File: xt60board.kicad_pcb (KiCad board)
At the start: 2 copper layers, 50.8 x 86.4 mm, 13 parts, among them J1 XT60, J10 XT60, J11 XT60, J12 XT60, J2 XT60, J3 XT60, J4 XT60, J5 XT60, J6 XT60, J7 XT60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

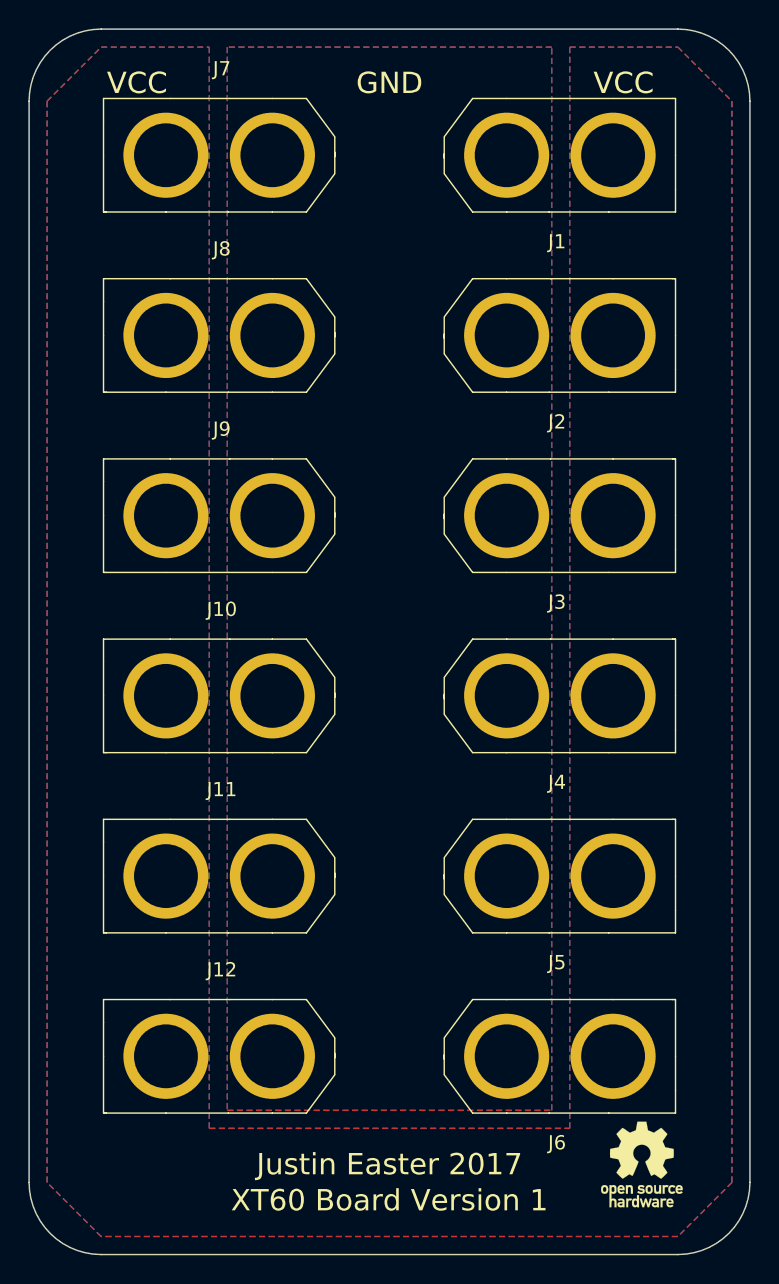
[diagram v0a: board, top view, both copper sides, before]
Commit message: Version 2
Shrank board size to reduce manufacturing cost.
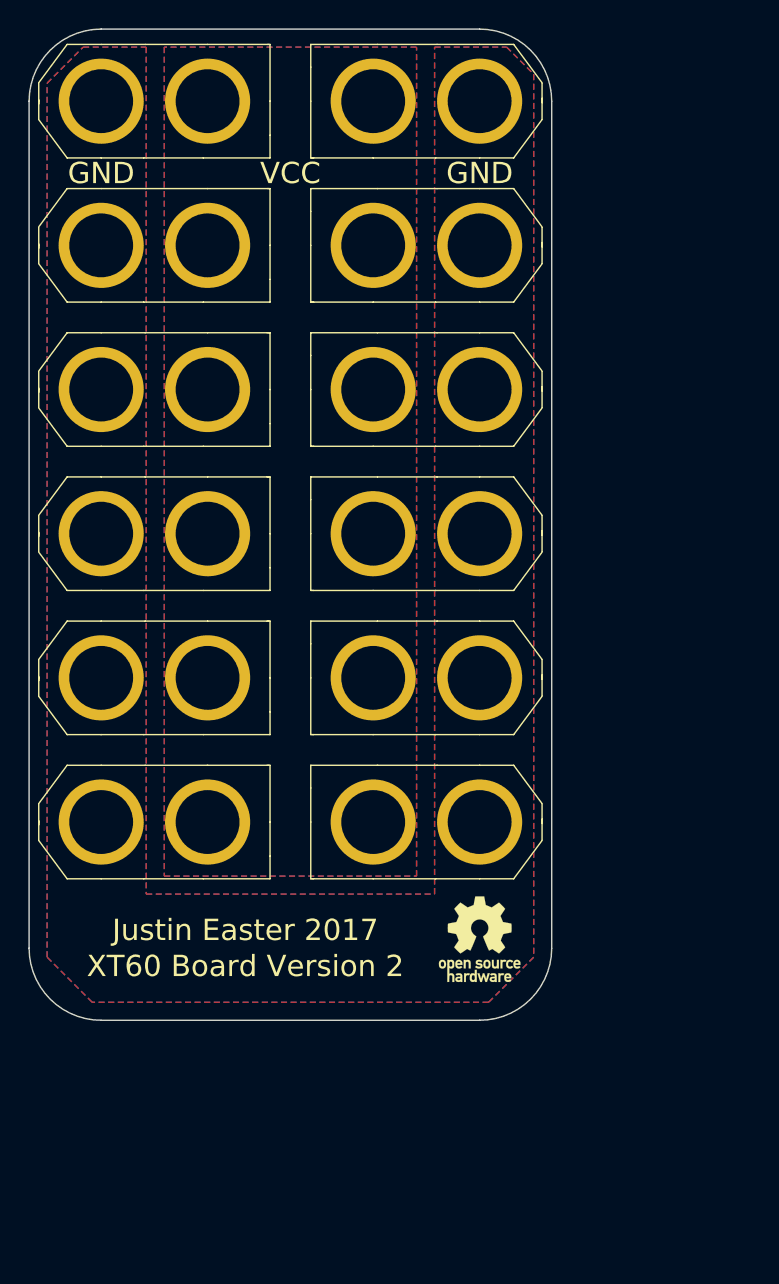
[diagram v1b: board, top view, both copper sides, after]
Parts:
- moved J12 20.4 mm to (114.3, 109.2), turned to 0 degrees
- moved REF*** 19.6 mm to (141.0, 117.5)
- moved J11 18.5 mm to (114.3, 99.1), turned to 0 degrees
- moved J6 16.6 mm to (141.0, 109.2), turned to 180 degrees
- moved J10 16.6 mm to (114.3, 88.9), turned to 0 degrees
- moved J9 15.0 mm to (114.3, 78.7), turned to 0 degrees
- moved J5 14.1 mm to (141.0, 99.1), turned to 180 degrees
- moved J8 13.6 mm to (114.3, 68.6), turned to 0 degrees
- moved J7 12.7 mm to (114.3, 58.4), turned to 0 degrees
- moved J4 11.6 mm to (141.0, 88.9), turned to 180 degrees
- moved J3 9.09 mm to (141.0, 78.7), turned to 180 degrees
- moved J2 6.63 mm to (141.0, 68.6), turned to 180 degrees
- moved J1 4.26 mm to (141.0, 58.4), turned to 180 degrees
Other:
- board size 50.8 x 86.4 mm -> 36.8 x 69.9 mm
- net class Thick added: clearance 0.2, trace_width 1, via_dia 0.6, via_drill 0.4
- board text added: "XT60 Board Version 2"
- board text removed: "XT60 Board Version 1"
